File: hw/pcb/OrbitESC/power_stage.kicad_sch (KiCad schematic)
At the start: 37 parts, among them U5 DRV8300DRGER, U6 TSV994

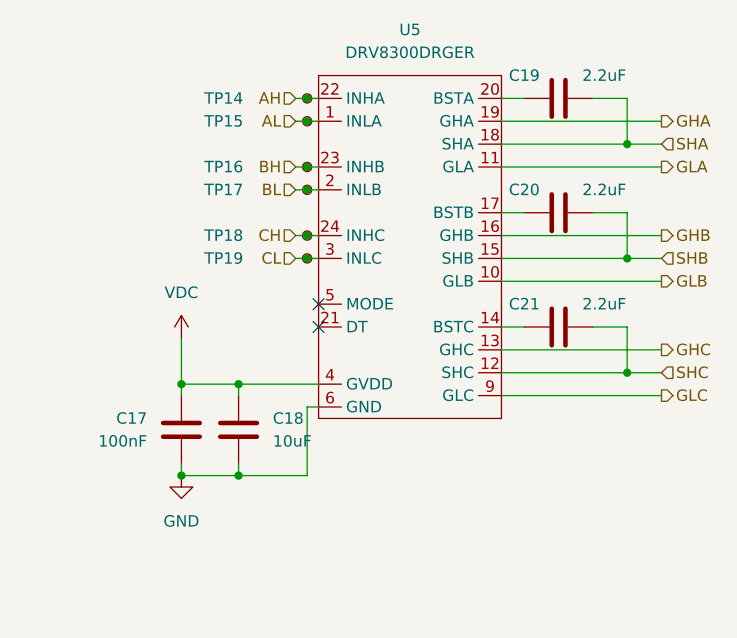
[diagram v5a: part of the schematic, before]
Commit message: Update PCB to match schematic
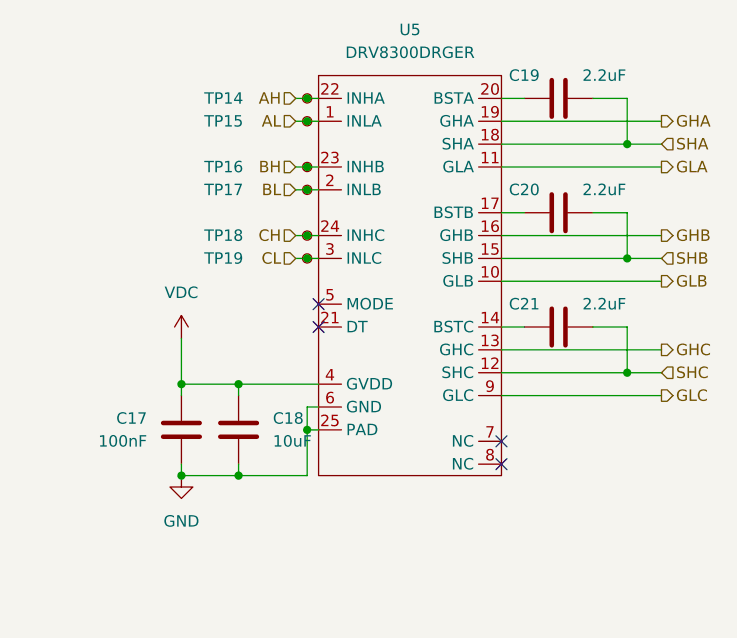
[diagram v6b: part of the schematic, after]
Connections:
- net GND: now also U5.25 (PAD)
- no-connect marks 2 -> 4
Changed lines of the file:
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@@
   (junction (at 134.62 165.186) (diameter 0) (color 0 0 0 0)
+  )
+  (junction (at 200.66 80.01) (diameter 0) (color 0 0 0 0)
   )
   (junction (at 60.96 165.186) (diameter 0) (color 0 0 0 0)
@@
   (no_connect (at 201.93 66.04))
   (no_connect (at 201.93 68.58))
+  (no_connect (at 222.25 81.28))
+  (no_connect (at 222.25 83.82))
   (wire (pts (xy 199.39 50.8) (xy 200.66 50.8))
     (stroke (width 0) (type default) (color 0 0 0 0))
@@
     (stroke (width 0) (type default) (color 0 0 0 0))
   )
-  (wire (pts (xy 200.66 85.09) (xy 200.66 77.47))
+  (wire (pts (xy 200.66 85.09) (xy 200.66 80.01))
     (stroke (width 0) (type default) (color 0 0 0 0))
   )
@@
     (stroke (width 0) (type default) (color 0 0 0 0))
   )
+  (wire (pts (xy 200.66 80.01) (xy 201.93 80.01))
+    (stroke (width 0) (type default) (color 0 0 0 0))
+  )
   (wire (pts (xy 222.25 60.96) (xy 236.22 60.96))
     (stroke (width 0) (type default) (color 0 0 0 0))
@@
   )
   (wire (pts (xy 60.96 176.616) (xy 60.96 179.156))
+    (stroke (width 0) (type default) (color 0 0 0 0))
+  )
+  (wire (pts (xy 200.66 80.01) (xy 200.66 77.47))
     (stroke (width 0) (type default) (color 0 0 0 0))
   )
@@
     (pin "23")
     (pin "24")
+    (pin "25")
     (pin "3")
     (pin "4")
     (pin "5")
     (pin "6")
+    (pin "7")
+    (pin "8")
     (pin "9")
   )

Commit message: Redo power stage layout. Start on power supplies
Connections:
- net IA: now also U6.1; no longer U6.7
- net IB: now also U6.7; no longer U6.8
- net IC: now also U6.8; no longer U6.1
- net at R25.2, R26.2: now also U6.9 (-); no longer U6.2 (-)
- net at R31.2, R32.2: now also U6.6 (-); no longer U6.9 (-)
- net at R34.2, R35.2: now also U6.2 (-); no longer U6.6 (-)
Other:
- moved on the sheet: U6A, U6B, U6C
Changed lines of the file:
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@@
     (pin "2")
   )
-  (symbol (lib_id "Amplifier_Operational:TSV994") (at 142.24 140.97 180) (unit 3)
-    (in_bom yes) (on_board yes) (fields_autoplaced)
-    (property "Reference" "U6" (id 0) (at 142.24 130.81 0))
-    (property "Value" "TSV994" (id 1) (at 142.24 133.35 0))
-    (property "Footprint" "Package_SO:TSSOP-14_4.4x5mm_P0.65mm" (id 2) (at 143.51 143.51 0)
-      (effects (font (size 1.27 1.27)) hide)
-    )
-    (property "Datasheet" "https://www.st.com/resource/en/datasheet/tsv994.pdf" (id 3) (at 140.97 146.05 0)
-      (effects (font (size 1.27 1.27)) hide)
-    )
-    (property "DigiKey" "497-6003-1-ND" (id 4) (at 142.24 140.97 0)
+  (symbol (lib_id "Amplifier_Operational:TSV994") (at 78.74 140.97 180) (unit 3)
+    (in_bom yes) (on_board yes) (fields_autoplaced)
+    (property "Reference" "U6" (id 0) (at 78.74 130.81 0))
+    (property "Value" "TSV994" (id 1) (at 78.74 133.35 0))
+    (property "Footprint" "Package_SO:TSSOP-14_4.4x5mm_P0.65mm" (id 2) (at 80.01 143.51 0)
+      (effects (font (size 1.27 1.27)) hide)
+    )
+    (property "Datasheet" "https://www.st.com/resource/en/datasheet/tsv994.pdf" (id 3) (at 77.47 146.05 0)
+      (effects (font (size 1.27 1.27)) hide)
+    )
+    (property "DigiKey" "497-6003-1-ND" (id 4) (at 78.74 140.97 0)
       (effects (font (size 1.27 1.27)) hide)
     )
@@
     (pin "2")
   )
-  (symbol (lib_id "Amplifier_Operational:TSV994") (at 78.74 140.97 180) (unit 1)
-    (in_bom yes) (on_board yes) (fields_autoplaced)
-    (property "Reference" "U6" (id 0) (at 78.74 130.81 0))
-    (property "Value" "TSV994" (id 1) (at 78.74 133.35 0))
-    (property "Footprint" "Package_SO:TSSOP-14_4.4x5mm_P0.65mm" (id 2) (at 80.01 143.51 0)
-      (effects (font (size 1.27 1.27)) hide)
-    )
-    (property "Datasheet" "https://www.st.com/resource/en/datasheet/tsv994.pdf" (id 3) (at 77.47 146.05 0)
-      (effects (font (size 1.27 1.27)) hide)
-    )
-    (property "DigiKey" "497-6003-1-ND" (id 4) (at 142.24 140.97 0)
+  (symbol (lib_id "Amplifier_Operational:TSV994") (at 205.74 140.97 180) (unit 1)
+    (in_bom yes) (on_board yes) (fields_autoplaced)
+    (property "Reference" "U6" (id 0) (at 205.74 130.81 0))
+    (property "Value" "TSV994" (id 1) (at 205.74 133.35 0))
+    (property "Footprint" "Package_SO:TSSOP-14_4.4x5mm_P0.65mm" (id 2) (at 207.01 143.51 0)
+      (effects (font (size 1.27 1.27)) hide)
+    )
+    (property "Datasheet" "https://www.st.com/resource/en/datasheet/tsv994.pdf" (id 3) (at 204.47 146.05 0)
+      (effects (font (size 1.27 1.27)) hide)
+    )
+    (property "DigiKey" "497-6003-1-ND" (id 4) (at 269.24 140.97 0)
       (effects (font (size 1.27 1.27)) hide)
     )
@@
     (pin "2")
   )
-  (symbol (lib_id "Amplifier_Operational:TSV994") (at 205.74 140.97 180) (unit 2)
-    (in_bom yes) (on_board yes) (fields_autoplaced)
-    (property "Reference" "U6" (id 0) (at 205.74 130.81 0))
-    (property "Value" "TSV994" (id 1) (at 205.74 133.35 0))
-    (property "Footprint" "Package_SO:TSSOP-14_4.4x5mm_P0.65mm" (id 2) (at 207.01 143.51 0)
-      (effects (font (size 1.27 1.27)) hide)
-    )
-    (property "Datasheet" "https://www.st.com/resource/en/datasheet/tsv994.pdf" (id 3) (at 204.47 146.05 0)
-      (effects (font (size 1.27 1.27)) hide)
-    )
-    (property "DigiKey" "497-6003-1-ND" (id 4) (at 142.24 140.97 0)
-      (effects (font (size 1.27 1.27)) hide)
-    )
+  (symbol (lib_id "Amplifier_Operational:TSV994") (at 142.24 140.97 180) (unit 2)
+    (in_bom yes) (on_board yes) (fields_autoplaced)
+    (property "Reference" "U6" (id 0) (at 142.24 130.81 0))
+    (property "Value" "TSV994" (id 1) (at 142.24 133.35 0))
+    (property "Footprint" "Package_SO:TSSOP-14_4.4x5mm_P0.65mm" (id 2) (at 143.51 143.51 0)
+      (effects (font (size 1.27 1.27)) hide)
+    )
+    (property "Datasheet" "https://www.st.com/resource/en/datasheet/tsv994.pdf" (id 3) (at 140.97 146.05 0)
+      (effects (font (size 1.27 1.27)) hide)
+    )
+    (property "DigiKey" "497-6003-1-ND" (id 4) (at 78.74 140.97 0)
+      (effects (font (size 1.27 1.27)) hide)
+    )
